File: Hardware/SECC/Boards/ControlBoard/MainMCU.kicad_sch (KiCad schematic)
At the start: 31 parts, among them U1 STM32H723ZGT6, Y1 8MHz

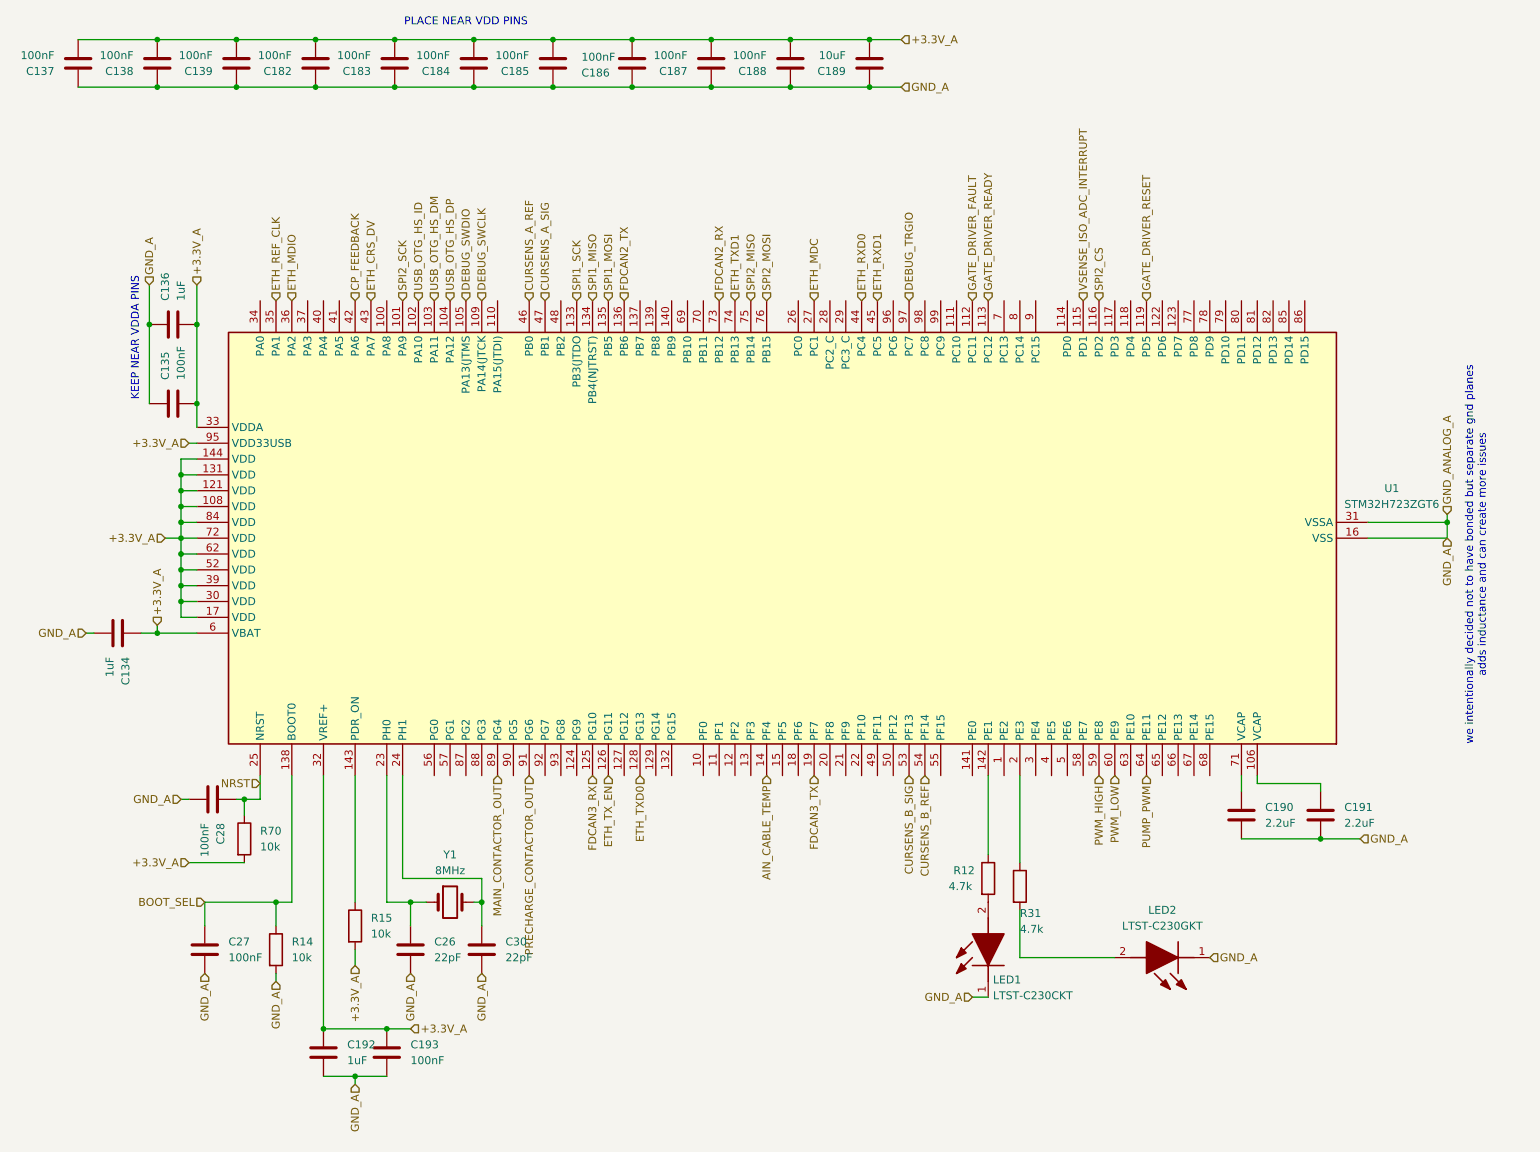
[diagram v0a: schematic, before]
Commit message: Update SECC Schematic
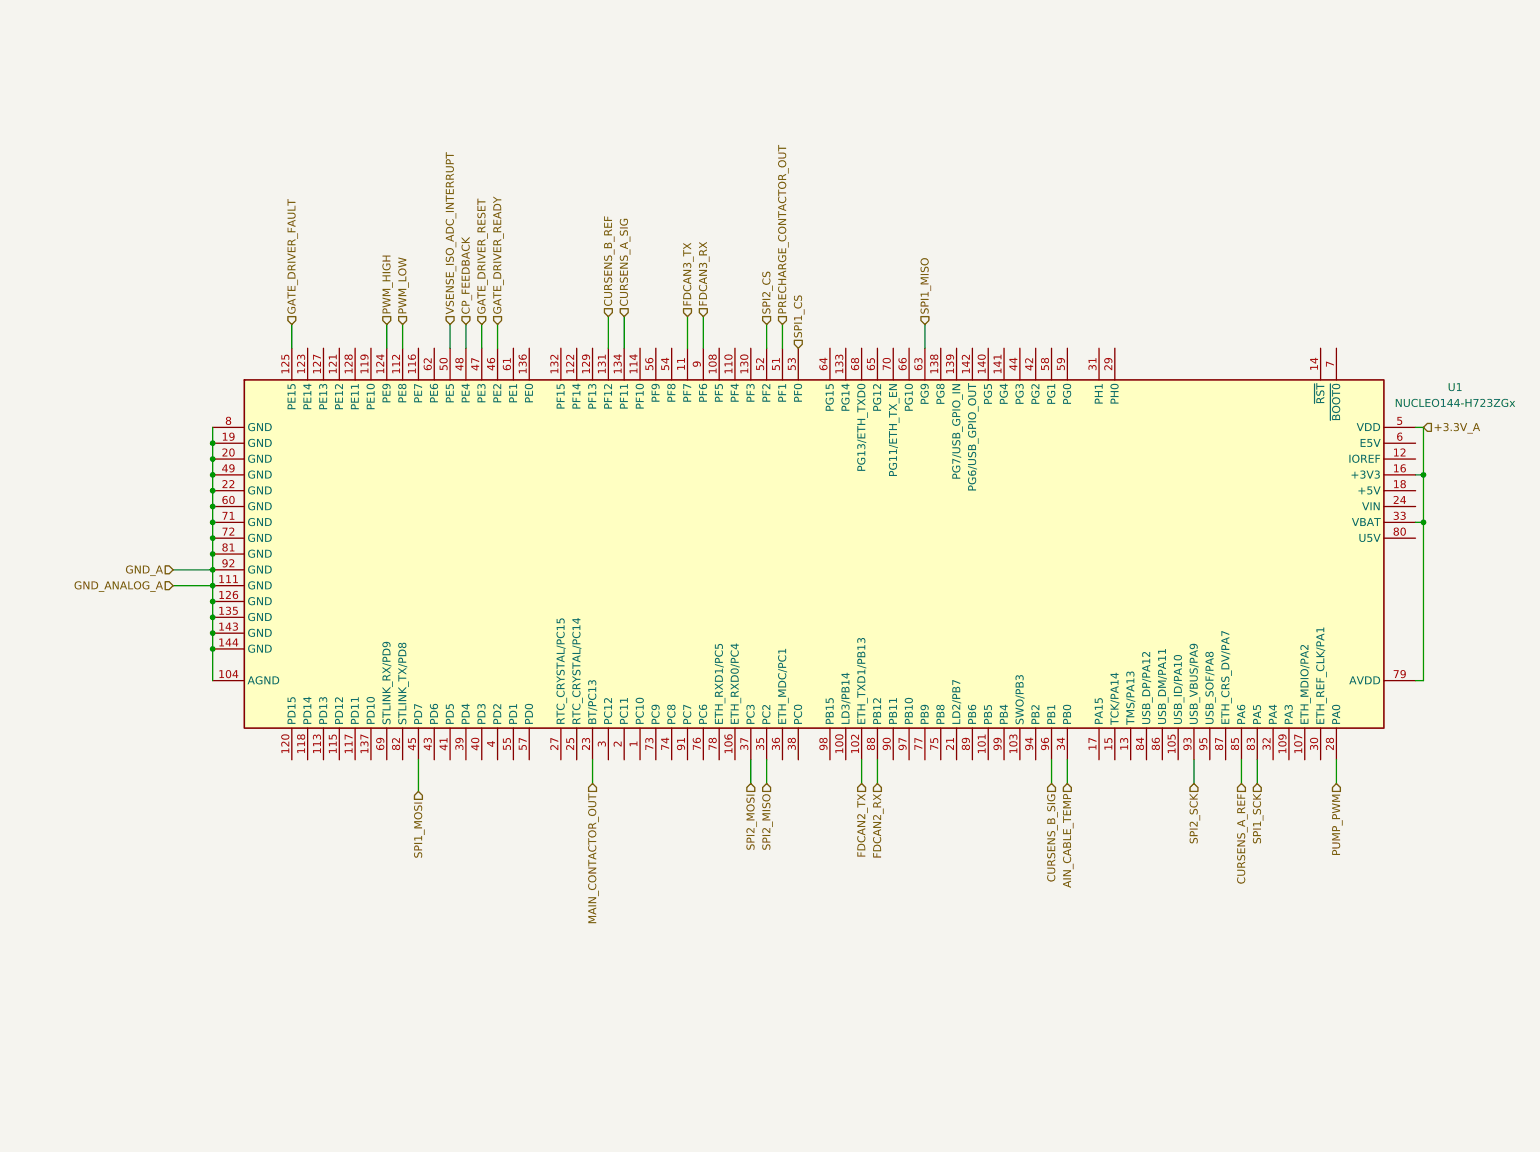
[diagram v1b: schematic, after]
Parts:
- removed C134, C136, C192: 1uF, Capacitor_SMD:C_1210_3225Metric_Pad1.33x2.70mm_HandSolder, symbol Device:C
- removed C135, C137, C138, C139, C182, C183, C184, C185, C186, C187, C188, C193, C27, C28: 100nF, Capacitor_SMD:C_1210_3225Metric_Pad1.33x2.70mm_HandSolder, symbol Device:C
- removed C189: 10uF, Capacitor_SMD:C_1210_3225Metric_Pad1.33x2.70mm_HandSolder, symbol Device:C
- removed C190, C191: 2.2uF, Capacitor_SMD:C_1210_3225Metric_Pad1.33x2.70mm_HandSolder, symbol Device:C
- removed C26, C30: 22pF, Capacitor_SMD:C_1210_3225Metric_Pad1.33x2.70mm_HandSolder, symbol Device:C
- removed LED1: LTST-C230CKT, InverterCom:LEDC3216X120N, symbol InverterCom:LTST-C230CKT
- removed LED2: LTST-C230GKT, InverterCom:LEDC3216X120N, symbol InverterCom:LTST-C230GKT
- removed R12, R31: 4.7k, Resistor_SMD:R_1210_3225Metric_Pad1.30x2.65mm_HandSolder, symbol Device:R
- removed R14, R15, R70: 10k, Resistor_SMD:R_1210_3225Metric_Pad1.30x2.65mm_HandSolder, symbol Device:R
- removed U1: STM32H723ZGT6, Package_QFP:LQFP-144_20x20mm_P0.5mm, symbol MCU_ST_STM32H7:STM32H723ZGTx
- removed Y1: 8MHz, Crystal:Crystal_HC49-4H_Vertical, symbol Device:Crystal
- added U1: NUCLEO144-H723ZGx, Module:ST_Morpho_Connector_144_STLink, symbol MCU_Module:NUCLEO144-H743ZI
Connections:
- net +3.3V_A: now also U1.16 (+3V3), U1.33 (VBAT), U1.5 (VDD), U1.79 (AVDD)
- net AIN_CABLE_TEMP: now also U1.34 (PB0)
- net CP_FEEDBACK: now also U1.48 (PE4)
- net CURSENS_A_REF: now also U1.85 (PA6)
- net CURSENS_A_SIG: now also U1.134 (PF11)
- net CURSENS_B_REF: now also U1.131 (PF12)
- net CURSENS_B_SIG: now also U1.96 (PB1)
- net FDCAN2_RX: now also U1.88 (PB12)
- net FDCAN2_TX: now also U1.102 (ETH_TXD1/PB13)
- net FDCAN3_RX: now also U1.9 (PF6)
- net FDCAN3_TX: now also U1.11 (PF7)
- net GATE_DRIVER_FAULT: now also U1.125 (PE15)
- net GATE_DRIVER_READY: now also U1.46 (PE2)
- net GATE_DRIVER_RESET: now also U1.47 (PE3)
- net GND_A: now also U1.104 (AGND), U1.111 (GND), U1.126 (GND), U1.135 (GND), U1.143 (GND), U1.144 (GND), U1.19 (GND), U1.20 (GND), U1.22 (GND), U1.49 (GND), U1.60 (GND), U1.71 (GND), U1.72 (GND), U1.8 (GND), U1.81 (GND), U1.92 (GND)
- net MAIN_CONTACTOR_OUT: now also U1.23 (BT/PC13)
- net PRECHARGE_CONTACTOR_OUT: now also U1.51 (PF1)
- net PUMP_PWM: now also U1.28 (PA0)
- net PWM_HIGH: now also U1.124 (PE9)
- net PWM_LOW: now also U1.112 (PE8)
- net SPI1_MISO: now also U1.63 (PG9)
- net SPI1_MOSI: now also U1.45 (PD7)
- net SPI1_SCK: now also U1.83 (PA5)
- net SPI2_CS: now also U1.52 (PF2)
- net SPI2_MISO: now also U1.35 (PC2)
- net SPI2_MOSI: now also U1.37 (PC3)
- net SPI2_SCK: now also U1.93 (USB_VBUS/PA9)
- net VSENSE_ISO_ADC_INTERRUPT: now also U1.50 (PE5)
- new net SPI1_CS: U1.53 (PF0)
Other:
- note removed: "KEEP NEAR VDDA PINS"
- note removed: "PLACE NEAR VDD PINS"
- note removed: "we intentionally decided not to have bonded but separate gnd planes adds inductance and can create more issues"

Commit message: Finish schematic
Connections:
- net REDBEET-GPIO2: now reaches U1.39 (PD4)
- net REDBEET-GPIO0: now reaches U1.4 (PD2)
- net REDBEET-GPIO1: now reaches U1.40 (PD3)
- net REDBEET-GPIO3: now reaches U1.41 (PD5)
- net SPI1_INTERRUPT: now reaches U1.55 (PD1)
- net REDBEET-RESET: now reaches U1.57 (PD0)
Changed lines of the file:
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@@
+		)
+	)
+	(hierarchical_label "SPI1_INTERRUPT"
+		(shape input)
+		(at 95.25 132.08 270)
+		(effects
+			(font
+				(size 1.27 1.27)
+			)
+			(justify right)
 		)
 	)
@@
 		)
 	)
+	(hierarchical_label "REDBEET-GPIO3"
+		(shape input)
+		(at 85.09 132.08 270)
+		(effects
+			(font
+				(size 1.27 1.27)
+			)
+			(justify right)
+		)
+	)
 	(hierarchical_label "CURSENS_A_REF"
 		(shape input)
@@
 		)
 	)
+	(hierarchical_label "REDBEET-RESET"
+		(shape input)
+		(at 97.79 132.08 270)
+		(effects
+			(font
+				(size 1.27 1.27)
+			)
+			(justify right)
+		)
+	)
 	(hierarchical_label "PWM_HIGH"
 		(shape input)
@@
 		)
 	)
+	(hierarchical_label "REDBEET-GPIO2"
+		(shape input)
+		(at 87.63 132.08 270)
+		(effects
+			(font
+				(size 1.27 1.27)
+			)
+			(justify right)
+		)
+	)
 	(hierarchical_label "SPI2_CS"
 		(shape input)
@@
 		)
 	)
+	(hierarchical_label "REDBEET-GPIO1"
+		(shape input)
+		(at 90.17 132.08 270)
+		(effects
+			(font
+				(size 1.27 1.27)
+			)
+			(justify right)
+		)
+	)
 	(hierarchical_label "FDCAN2_RX"
 		(shape input)
@@
 		)
 	)
+	(hierarchical_label "REDBEET-GPIO0"
+		(shape input)
+		(at 92.71 132.08 270)
+		(effects
+			(font
+				(size 1.27 1.27)
+			)
+			(justify right)
+		)
+	)

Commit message: esp32 stuff
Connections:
- net CP_FEEDBACK: now also U1.129 (PF13); no longer U1.48 (PE4)
- net FDCAN1_TX: now reaches U1.84 (USB_DP/PA12)
- net FDCAN1_RX: now reaches U1.86 (USB_DM/PA11)
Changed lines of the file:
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@@
+	(wire
+		(pts
+			(xy 107.95 60.96) (xy 107.95 66.04)
+		)
+		(stroke
+			(width 0)
+			(type default)
+		)
+	)
 	(wire
 		(pts
@@
 	(wire
 		(pts
-			(xy 87.63 62.23) (xy 87.63 66.04)
+			(xy 196.85 132.08) (xy 196.85 135.89)
 		)
 		(stroke
@@
 	(wire
 		(pts
+			(xy 199.39 132.08) (xy 199.39 135.89)
+		)
+		(stroke
+			(width 0)
+			(type default)
+		)
+	)
+	(wire
+		(pts
 			(xy 204.47 132.08) (xy 204.47 135.89)
 		)
@@
 		)
 	)
+	(hierarchical_label "FDCAN1_RX"
+		(shape input)
+		(at 199.39 135.89 270)
+		(effects
+			(font
+				(size 1.27 1.27)
+			)
+			(justify right)
+		)
+	)
 	(hierarchical_label "SPI1_CS"
 		(shape input)
@@
 		)
 	)
+	(hierarchical_label "FDCAN1_TX"
+		(shape input)
+		(at 196.85 135.89 270)
+		(effects
+			(font
+				(size 1.27 1.27)
+			)
+			(justify right)
+		)
+	)
 	(hierarchical_label "REDBEET-GPIO1"
 		(shape input)
@@
 	(hierarchical_label "CP_FEEDBACK"
 		(shape input)
-		(at 87.63 62.23 90)
-		(effects
-			(font
+		(at 107.95 60.96 90)
+		(effects
+			(font
